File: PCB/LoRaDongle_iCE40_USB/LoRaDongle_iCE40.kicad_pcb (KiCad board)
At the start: 4 copper layers, 110 x 45 mm, 137 parts, among them IC1 93LC56BT-I_OT, IC2 ICE40UP5K-UWG30ITR1K, IC3 N25Q032A13ESC40F, J1 USB_A, J10 Jumper_2_Open, J2 Conn_01x08, J3 Conn_02x02_Top_Bottom, J4 Jumper, J5 142-0701-801, J6 Conn_01x06, J7 Jumper_NC_Small, J8 Jumper, J9 Conn_02x02_Top_Bottom, U1 RP550K001A-TR, U2 FT232H, U3 SX1261IMLTRT, U4 SKY13587-378LF, X1 ECS-2520MV-500-BL-TR, Y1 Crystal_GND24_Small, Y2 Crystal_GND24

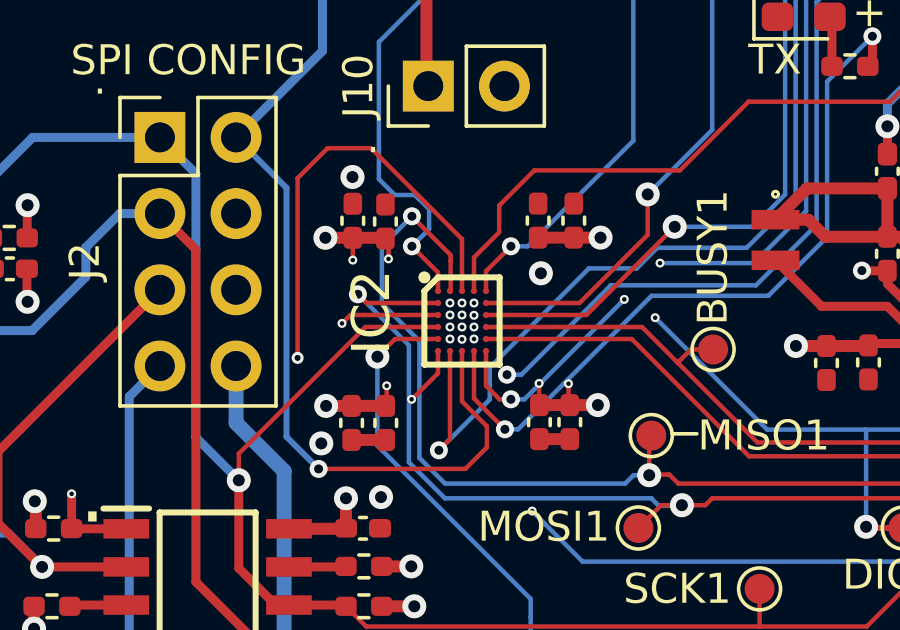
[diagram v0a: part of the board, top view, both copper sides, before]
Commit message: updated ftdi and flash chip, removed xilinx project
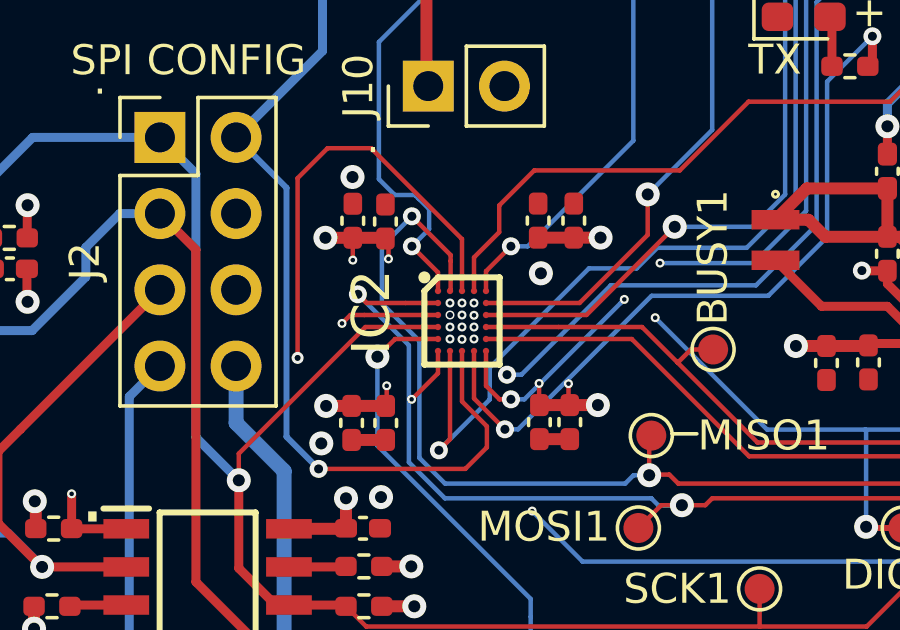
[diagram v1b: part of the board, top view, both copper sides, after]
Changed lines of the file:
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@@
   (via (at 134.96 115.9) (size 1) (drill 0.5) (layers "F.Cu" "B.Cu") (net 95))
   (via micro (at 155.67 96.89) (size 0.3) (drill 0.15) (layers "F.Cu" "In1.Cu") (net 95))
-  (via micro (at 155.67 97.29) (size 0.3) (drill 0.15) (layers "F.Cu" "In1.Cu") (net 95))
+  (via micro (at 155.67 97.29) (size 0.3) (drill 0.2) (layers "F.Cu" "In1.Cu") (net 95))
   (via micro (at 152.43 95.46) (size 0.3) (drill 0.15) (layers "F.Cu" "In1.Cu") (net 95))
   (via micro (at 153.62 95.42) (size 0.3) (drill 0.15) (layers "F.Cu" "In1.Cu") (net 95))

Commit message: updated layout and routing
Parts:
- removed 5V0: 5V, TestPoint:TestPoint_Pad_D1.0mm
- removed BUSY1: Radio_Busy, TestPoint:TestPoint_Pad_D1.0mm
- removed CDNE1: iCE_CDONE, TestPoint:TestPoint_Pad_D1.0mm
- removed CLK1: CLK, TestPoint:TestPoint_Pad_D1.0mm
- removed CRST1: iCE_CRESET, TestPoint:TestPoint_Pad_D1.0mm
- removed CS#1: CS#, TestPoint:TestPoint_Pad_D1.0mm
- removed CTL1: CTL1, TestPoint:TestPoint_Pad_D1.0mm
- removed DIO1: Radio_DIO1, TestPoint:TestPoint_Pad_D1.0mm
- removed Data1: Data, TestPoint:TestPoint_Pad_D1.0mm
- removed J10: Jumper_2_Open, Connector_PinHeader_2.54mm:PinHeader_1x02_P2.54mm_Vertical
- removed J9: Conn_02x02_Top_Bottom, Connector_PinHeader_2.54mm:PinHeader_2x02_P2.54mm_Vertical
- removed L_SS1: LoRa_!SS, TestPoint:TestPoint_Pad_D1.0mm
- removed MISO1: LoRA_MISO, TestPoint:TestPoint_Pad_D1.0mm
- removed MOSI1: LoRa_MOSI, TestPoint:TestPoint_Pad_D1.0mm
- removed REF**: OSHW-Symbol_6.7x6mm_SilkScreen, Symbol:OSHW-Symbol_6.7x6mm_SilkScreen
- removed REF**: KiCad-Logo2_5mm_SilkScreen, Symbol:KiCad-Logo2_5mm_SilkScreen
- removed RESET1: LoRA_~RESET, TestPoint:TestPoint_Pad_D1.0mm
- removed SCK1: LoRa_SCK, TestPoint:TestPoint_Pad_D1.0mm
- removed SS_B1: iCE_SS_B, TestPoint:TestPoint_Pad_D1.0mm
- added C53: 3.3uF, Capacitor_SMD:C_0603_1608Metric_Pad1.08x0.95mm_HandSolder, F.Cu at (133.9, 91.3)
- added C54: 1uF, Capacitor_SMD:C_0402_1005Metric_Pad0.74x0.62mm_HandSolder, F.Cu at (137.7, 131.2)
- added C55: 1uF, Capacitor_SMD:C_0402_1005Metric_Pad0.74x0.62mm_HandSolder, F.Cu at (142.6, 132.8)
- added JP1: SolderJumper_2_Open, Resistor_SMD:R_0603_1608Metric_Pad0.98x0.95mm_HandSolder, F.Cu at (132.2, 114.3)
- added JP2: SolderJumper_2_Open, Resistor_SMD:R_0603_1608Metric_Pad0.98x0.95mm_HandSolder, F.Cu at (125.3, 115.1)
- added JP3: SolderJumper_2_Open, Resistor_SMD:R_0603_1608Metric_Pad0.98x0.95mm_HandSolder, F.Cu at (125.3, 116.7)
- added OSCI1: OSCI, TestPoint:TestPoint_Pad_D2.5mm, F.Cu at (113.9, 83.6)
- added OSCO1: OSCO, TestPoint:TestPoint_Pad_D2.5mm, F.Cu at (111.7, 89.2)
- added R22: 10K, Resistor_SMD:R_0402_1005Metric_Pad0.72x0.64mm_HandSolder, F.Cu at (119.7, 83.0)
- added R23: 10K, Resistor_SMD:R_0402_1005Metric_Pad0.72x0.64mm_HandSolder, F.Cu at (120.7, 81.2)
- added R24: 10K, Resistor_SMD:R_0402_1005Metric_Pad0.72x0.64mm_HandSolder, F.Cu at (148.0, 107.6)
- added R25: 10K, Resistor_SMD:R_0402_1005Metric_Pad0.72x0.64mm_HandSolder, F.Cu at (137.0, 132.8)
- added R26: 4.7, Resistor_SMD:R_0402_1005Metric_Pad0.72x0.64mm_HandSolder, F.Cu at (137.0, 129.6)
- added R27: 10K, Resistor_SMD:R_0402_1005Metric_Pad0.72x0.64mm_HandSolder, F.Cu at (143.1, 131.2)
- added SW2: SW_Push, Button_Switch_THT:SW_PUSH_6mm_H5mm, F.Cu at (150.6, 114.7)
- added U5: W25Q128JVS, Package_SO:SOIC-8_5.23x5.23mm_P1.27mm, F.Cu at (127.7, 110.6)
- added XTA1: XTA, TestPoint:TestPoint_Pad_D2.5mm, F.Cu at (161.0, 81.5)
- added XTB1: XTB, TestPoint:TestPoint_Pad_D2.5mm, F.Cu at (156.0, 80.0)
- added iCE_CLK1: iCE_CLK, TestPoint:TestPoint_Pad_D2.5mm, F.Cu at (148.6, 89.1)
- 1V2, 3V3, CTL2, GND1, GND2, iCE_SI1, iCE_SO1: footprint TestPoint:TestPoint_Pad_D1.0mm -> TestPoint:TestPoint_Pad_D2.5mm
- C10: value 10nF -> 0.1uF
- D1: footprint LED_SMD:LED_0805_2012Metric_Pad1.15x1.40mm_HandSolder -> LED_SMD:LED_0603_1608Metric
- IC3: value N25Q032A13ESC40F -> SGP40-D-R4; footprint N25Q032A13ESC40F:SOIC127P600X175-8N -> KiCad_SGP40-D-R4:SON80P244X244X95-7N
- J3: value Conn_02x02_Top_Bottom -> Conn_01x08_Male; footprint Connector_PinHeader_2.54mm:PinHeader_2x02_P2.54mm_Vertical -> Connector_PinHeader_2.54mm:PinHeader_2x04_P2.54mm_Vertical
- J4: value Jumper -> Conn_01x04_Male; footprint Connector_PinHeader_2.54mm:PinHeader_1x03_P2.54mm_Vertical -> Connector_PinHeader_2.54mm:PinHeader_1x04_P2.54mm_Vertical
- J6: value Conn_01x06 -> Conn_02x02_Top_Bottom; footprint Connector_PinHeader_2.54mm:PinHeader_1x06_P2.54mm_Vertical -> Connector_PinHeader_2.54mm:PinHeader_2x02_P2.54mm_Vertical
- J7: value Jumper_NC_Small -> Conn_01x03_Male; footprint Connector_PinHeader_2.54mm:PinHeader_1x02_P2.54mm_Vertical -> Connector_PinHeader_2.54mm:PinHeader_1x03_P2.54mm_Vertical
- J8: value Jumper -> Jumper_2_Open
- R8: value 10K -> 1K
- U2: value FT232H -> FT2232HL; footprint Package_QFP:LQFP-48_7x7mm_P0.5mm -> Package_QFP:LQFP-64_10x10mm_P0.5mm
- moved GND2 49.5 mm to (159.6, 106.8), turned to 0 degrees
- moved J2 39.4 mm to (129.6, 127.2)
- moved J6 38.5 mm to (144.0, 114.1), turned to 180 degrees
- moved J4 34.3 mm to (136.1, 138.8), turned to 90 degrees
- moved 1V2 34.1 mm to (116.0, 115.0), turned to 0 degrees
- moved J7 33.8 mm to (130.8, 79.6)
- moved C32 32.2 mm to (121.6, 112.5), turned to 0 degrees
- moved R16 31.7 mm to (121.6, 111.2)
- moved R17 31.3 mm to (121.6, 109.9), turned to 180 degrees
- moved L1 28.5 mm to (112.9, 109.6), turned to 90 degrees
- moved 3V3 27.9 mm to (150.0, 78.3), turned to 180 degrees
- moved L2 27.9 mm to (114.5, 109.6), turned to -90 degrees
- moved C2 27.8 mm to (110.4, 110.5), turned to 0 degrees
- moved IC3 26.8 mm to (140.1, 132.0)
- moved C6 24.8 mm to (117.1, 110.5), turned to 180 degrees
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- renumbered RESET to SW1
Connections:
- C1 pad 2: /V_USB -> +5V
- C10 pad 2: /USB_Interface/~{RESET} -> 1V8
- C13 pad 1: Net-(C13-Pad1) -> GND
- C13 pad 2: GND -> 1V8
- C16 pad 1: Net-(C16-Pad1) -> GND
- C16 pad 2: GND -> 1V8
- FB1 pad 2: /V_USB -> +5V
- IC1 pad 5: /USB_Interface/CS# -> Net-(IC1-Pad5)
- IC2 pad A1: /ice40up5k_circuit/Pin_0 -> /RF Circuitry/LoRa_SCK
- IC2 pad A5: /ice40up5k_circuit/Pin_1 -> /ice40up5k_circuit/i2C_SDA
- IC2 pad B5: /ice40up5k_circuit/Pin_2 -> /ice40up5k_circuit/i2C_SCL
- IC2 pad C5: /ice40up5k_circuit/Pin_3 -> /ice40up5k_circuit/CPU_RESET
- IC2 pad F2: /ice40up5k_circuit/Pin_4 -> /USB_Interface/UART_USB_RX
- IC2 pad F5: /ice40up5k_circuit/Pin_5 -> /USB_Interface/UART_USB_TX
- IC3 pad 1: Net-(IC3-Pad1) -> Net-(C54-Pad1)
- IC3 pad 2: /SPI_MISO -> GND
- IC3 pad 3: Net-(IC3-Pad3) -> /ice40up5k_circuit/i2C_SDA
- IC3 pad 5: /SPI_MOSI -> 3V3
- IC3 pad 6: /SPI_SCK -> /ice40up5k_circuit/i2C_SCL
- IC3 pad 7: Net-(IC3-Pad7) -> GND
- J2 pad 8: /V_conn -> +5V
- J3 pad 1: /SPI_MOSI -> /RF Circuitry/LoRa_SCK
- J3 pad 2: /ice40up5k_circuit/iCE_SI -> /RF Circuitry/LoRa_MOSI
- J3 pad 3: /ice40up5k_circuit/iCE_SO -> /RF Circuitry/LoRa_MISO
- J3 pad 4: /SPI_MISO -> /RF Circuitry/LoRa_!SS
- J4 pad 1: /V_USB -> /ice40up5k_circuit/i2C_SDA
- J4 pad 2: +5V -> /ice40up5k_circuit/i2C_SCL
- J4 pad 3: /V_conn -> GND
- J6 pad 1: /ice40up5k_circuit/Pin_0 -> 3V3
- J6 pad 2: /ice40up5k_circuit/Pin_1 -> 1V2
- J6 pad 3: /ice40up5k_circuit/Pin_2 -> 3V3FPGA
- J6 pad 4: /ice40up5k_circuit/Pin_3 -> 1V2FPGA
- J7 pad 1: Net-(IC3-Pad1) -> /USB_Interface/DATA
- J7 pad 2: /SPI_SS -> /USB_Interface/CLK
- R14 pad 2: Net-(IC3-Pad3) -> Net-(R14-Pad2)
- R15 pad 1: Net-(IC3-Pad1) -> Net-(JP1-Pad2)
- R16 pad 1: Net-(IC3-Pad7) -> 3V3
- R16 pad 2: 3V3 -> Net-(R16-Pad2)
- R8 pad 1: /USB_Interface/~{RESET} -> Net-(R8-Pad1)
- U2 pad 1: Net-(C14-Pad1) -> GND
- U2 pad 12: 3V3 -> 1V8
- U2 pad 13: /SPI_SCK -> GND
- U2 pad 14: /SPI_MOSI -> Net-(R8-Pad1)
- U2 pad 15: /SPI_MISO -> GND
- U2 pad 16: unconnected-(U2-Pad16) -> /SPI_SCK
- U2 pad 17: /SPI_SS -> /SPI_MOSI
- U2 pad 18: unconnected-(U2-Pad18) -> /SPI_MISO
- U2 pad 19: /ICE_CDONE -> unconnected-(U2-Pad19)
- U2 pad 2: Net-(C15-Pad1) -> Net-(C14-Pad1)
- U2 pad 20: /ICE_CRESET -> 3V3
- U2 pad 21: unconnected-(U2-Pad21) -> /SPI_SS
- U2 pad 22: GND -> unconnected-(U2-Pad22)
- U2 pad 23: GND -> /ICE_CDONE
- U2 pad 24: 3V3 -> /ICE_CRESET
- U2 pad 25: unconnected-(U2-Pad25) -> GND
- U2 pad 3: /USB_Interface/VPHY -> Net-(C15-Pad1)
- U2 pad 31: unconnected-(U2-Pad31) -> 3V3
- U2 pad 34: /USB_Interface/~{RESET} -> unconnected-(U2-Pad34)
- U2 pad 36: GND -> unconnected-(U2-Pad36)
- U2 pad 37: Net-(C13-Pad1) -> 1V8
- U2 pad 38: Net-(C16-Pad1) -> /USB_Interface/UART_USB_TX
- U2 pad 39: 3V3 -> /USB_Interface/UART_USB_RX
- U2 pad 4: GND -> /USB_Interface/VPHY
- U2 pad 40: 3V3 -> unconnected-(U2-Pad40)
- U2 pad 41: GND -> unconnected-(U2-Pad41)
- U2 pad 42: GND -> 3V3
- U2 pad 43: /USB_Interface/DATA -> unconnected-(U2-Pad43)
- U2 pad 44: /USB_Interface/CLK -> unconnected-(U2-Pad44)
- U2 pad 45: /USB_Interface/CS# -> unconnected-(U2-Pad45)
- U2 pad 46: 3V3 -> unconnected-(U2-Pad46)
- U2 pad 48: GND -> unconnected-(U2-Pad48)
- U2 pad 5: Net-(R11-Pad1) -> GND
- U2 pad 6: /USB_Interface/USB_D- -> Net-(R11-Pad1)
- U2 pad 7: /USB_Interface/USB_D+ -> /USB_Interface/USB_D-
- U2 pad 8: /USB_Interface/VPLL -> /USB_Interface/USB_D+
- U2 pad 9: GND -> /USB_Interface/VPLL
- U3 pad 18: /SPI_SCK -> /RF Circuitry/LoRa_SCK
- X1 pad 3: Net-(J10-Pad1) -> /ice40up5k_circuit/iCE_CLK
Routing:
- net /SPI_SCK: track 80.6 -> 4.35 mm, vias 2 -> 0
- net /ICE_CRESET: track 77.7 -> 9.49 mm, vias 2 -> 1
- net 1V2FPGA: track 80.0 -> 12.2 mm, vias 7 -> 6
- net 3V3FPGA: track 95.9 -> 34.3 mm, vias 10 -> 9
- net /SPI_MISO: track 65.2 -> 8.23 mm, vias 2 -> 0
- net /V_conn: track 50.6 -> 0.00 mm
- net 1V2: track 57.6 -> 12.0 mm, vias 1 -> 0
- net /SPI_SS: track 49.2 -> 6.86 mm, vias 1 -> 3
- net /RF Circuitry/ANT_SW: track 42.2 -> 2.31 mm
- net /SPI_MOSI: track 47.3 -> 7.96 mm, vias 1 -> 0
- net GND: track 210.8 -> 173.9 mm, vias 80 -> 64
- net /ice40up5k_circuit/Pin_4: track 35.6 -> 0.00 mm, vias 1 -> 0
- net /ice40up5k_circuit/Pin_5: track 33.5 -> 0.00 mm, vias 3 -> 0
- net /ICE_CDONE: track 39.5 -> 8.59 mm, vias 4 -> 2
- net +5V: track 63.7 -> 32.9 mm
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- removed copper zone on In2.Cu, net 3V3
- removed copper zone on B.Cu, net GND
- removed copper zone on F.Cu, net GND
- removed copper zone on In1.Cu, net GND
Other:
- board size 110 x 45 mm -> 95 x 67 mm
- board text removed: "EXTERNAL"
- board text removed: "PWR SELECT"
- board text removed: "SELECT FLASH"
- board text removed: "SPI CONFIG"
- board text removed: "USB"

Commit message: updated routing
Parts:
- moved iCE_SI1 2.52 mm to (144.5, 106.4)
- moved iCE_SO1 1.57 mm to (139.5, 107.0)
- moved OSCI1 1.33 mm to (115.2, 83.7)
- moved OSCO1 0.63 mm to (112.0, 88.6)
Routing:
- net /USB_Interface/USB_D+: track 0.00 -> 15.3 mm
- net /SPI_SS: track 6.86 -> 21.1 mm
- net /USB_Interface/USB_D-: track 0.00 -> 12.8 mm, vias 0 -> 2
- net /SPI_MISO: track 8.23 -> 20.4 mm
- net /USB_Interface/CLK: track 18.6 -> 30.6 mm
- net GND: track 173.9 -> 185.2 mm, vias 64 -> 69
- net /SPI_SCK: track 4.35 -> 13.1 mm
- net Net-(C14-Pad1): track 1.85 -> 10.0 mm
- net Net-(C15-Pad1): track 0.00 -> 8.16 mm
- net /SPI_MOSI: track 7.96 -> 15.0 mm
- net Net-(IC1-Pad5): track 11.5 -> 18.5 mm
- net /USB_Interface/DATA: track 16.8 -> 22.9 mm
- net /ICE_CDONE: track 8.59 -> 14.4 mm, vias 2 -> 4
- net /D-: track 0.00 -> 3.96 mm
- net /D+: track 0.00 -> 3.94 mm
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- added copper zone on In1.Cu, net GND
